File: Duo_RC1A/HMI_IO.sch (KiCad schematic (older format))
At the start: 45 parts, among them P5 PIN_ARRAY_4X1

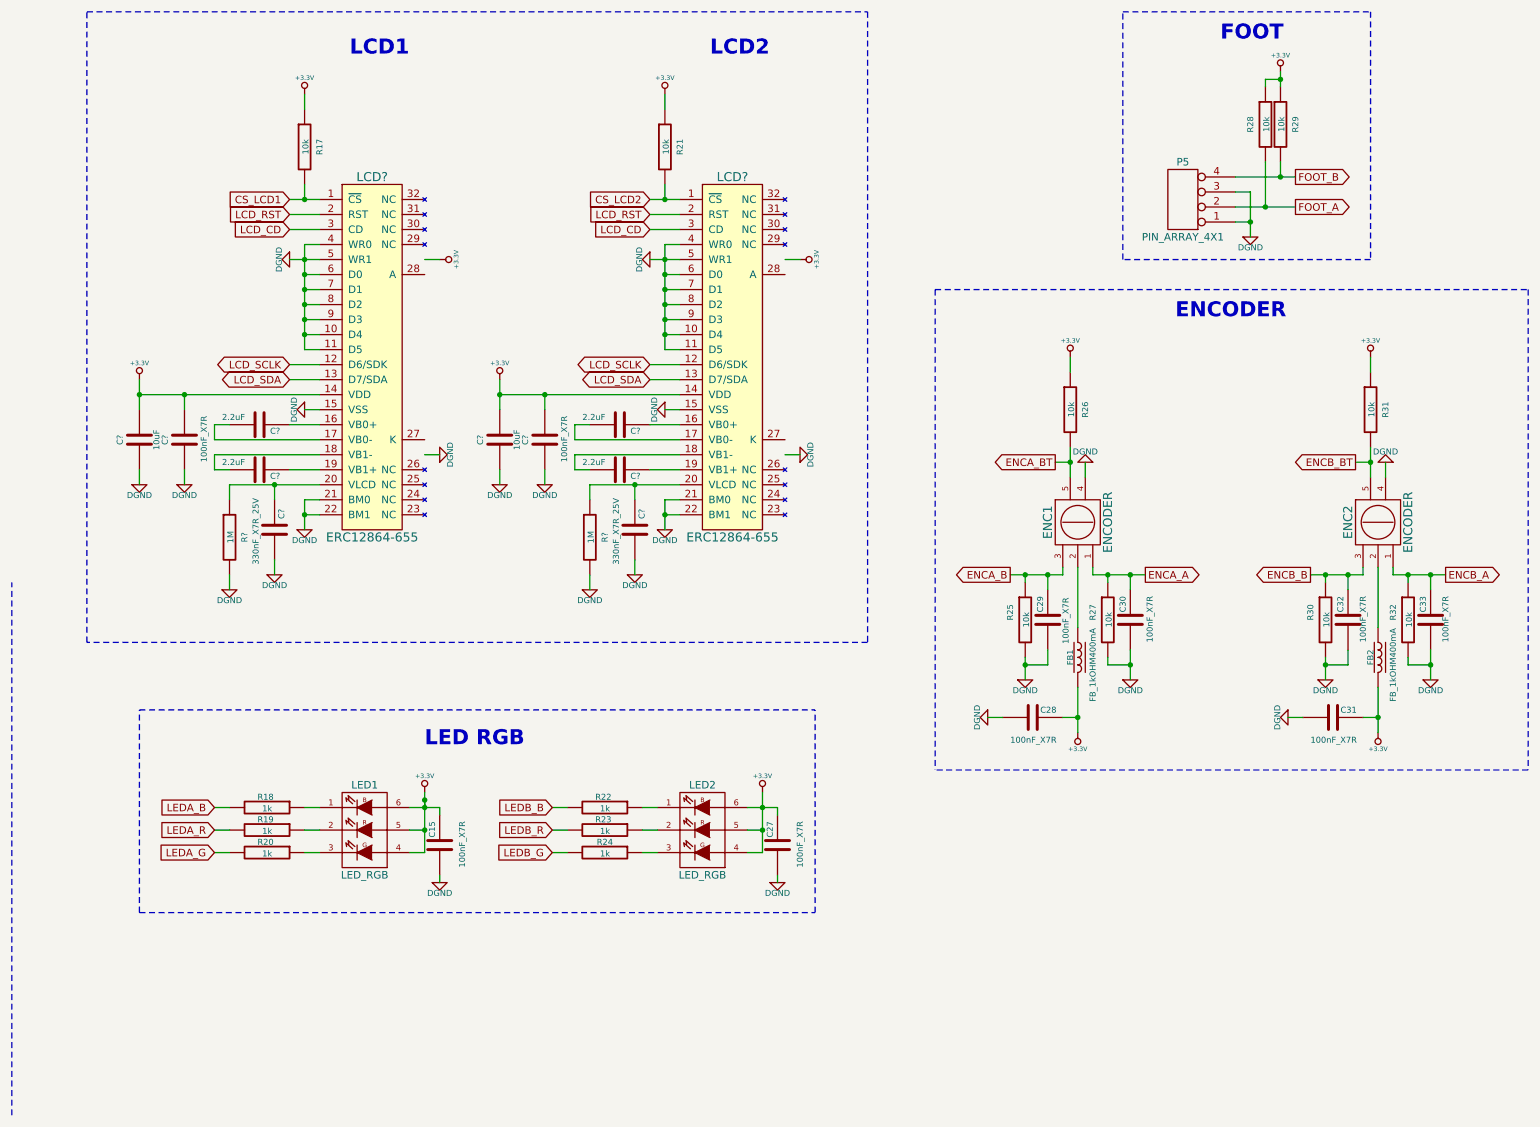
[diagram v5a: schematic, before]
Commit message: Changed the LCD for the 2.8pol. Rotated the bottom board connector. Moved the 3.3V linear regulator from the bottom board to the top board, and changed the power for the top board from 3.3V to 9V.
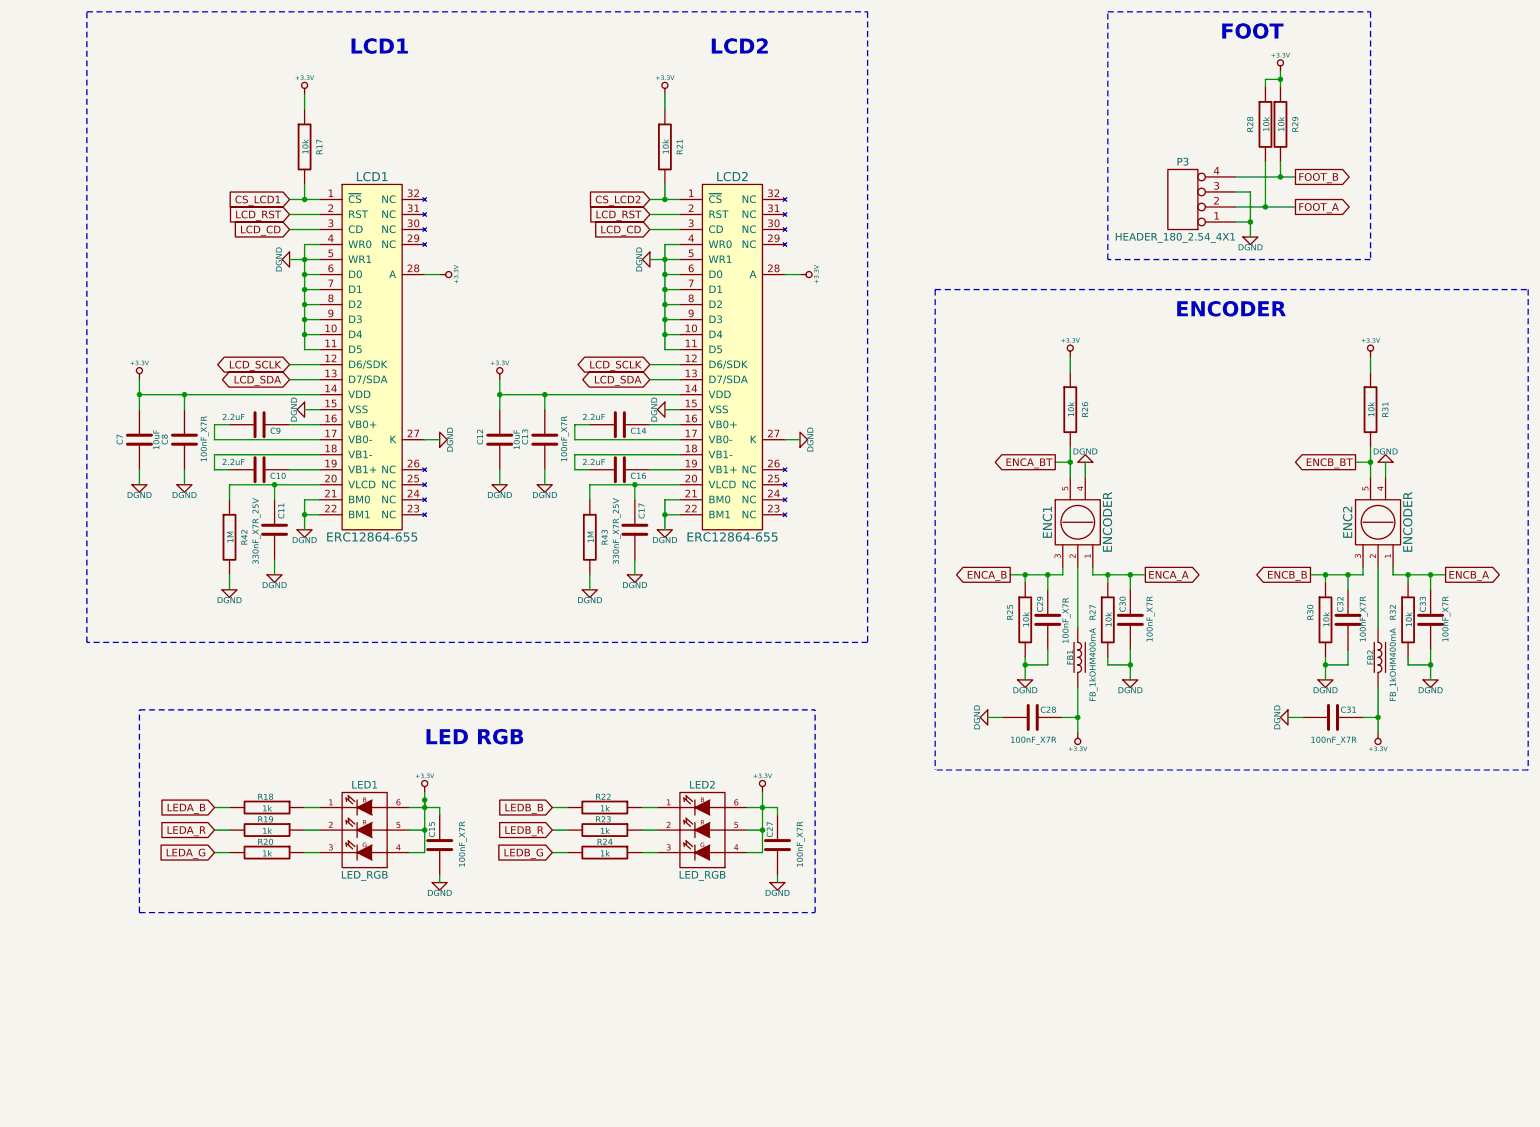
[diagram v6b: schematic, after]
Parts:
- C12, C7: renamed from C?; footprint Duo_Audio_HMI_RC1A:SM0805 -> Duo_Audio_HMI_RC1A:SM0603
- LCD1, LCD2: renamed from LCD?; footprint (none) -> Duo_Audio_HMI_RC1A:ERC12864-655
- P3: renamed from P5; value PIN_ARRAY_4X1 -> HEADER_180_2.54_4X1
- gave numbers to parts that had none: 10
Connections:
- net +3.3V: now also LCD1.28 (A), LCD2.28 (A)
- net DGND: now also LCD1.27 (K), LCD2.27 (K)
